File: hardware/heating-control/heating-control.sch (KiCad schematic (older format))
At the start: 10 parts

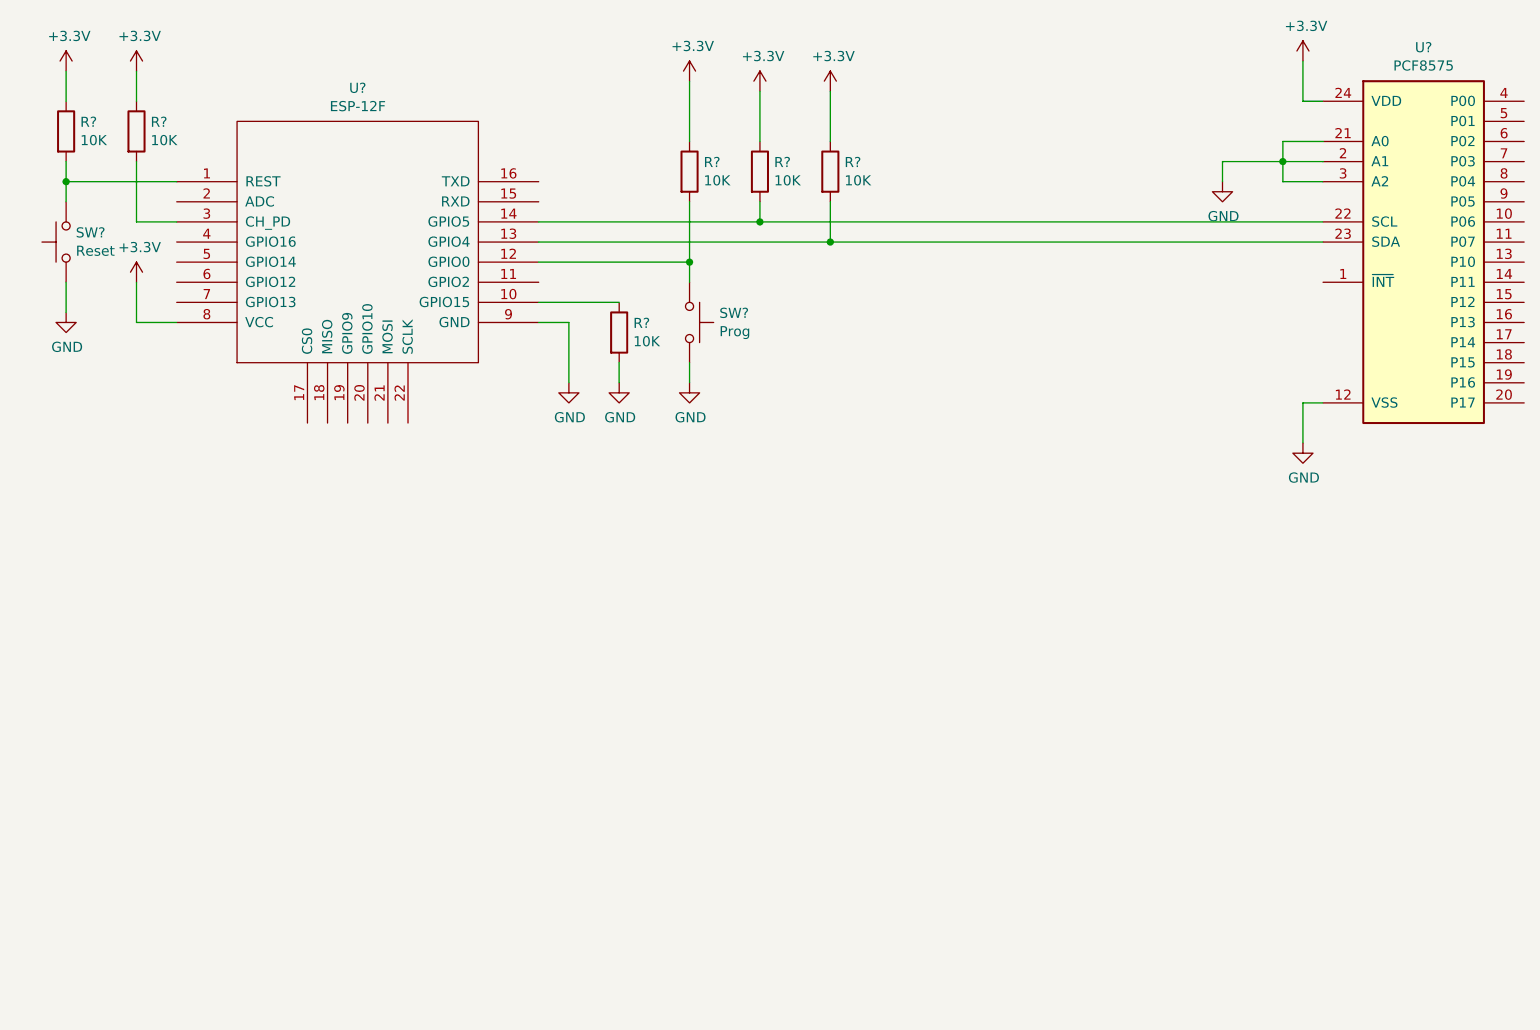
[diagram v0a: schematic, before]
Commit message: added programming interface
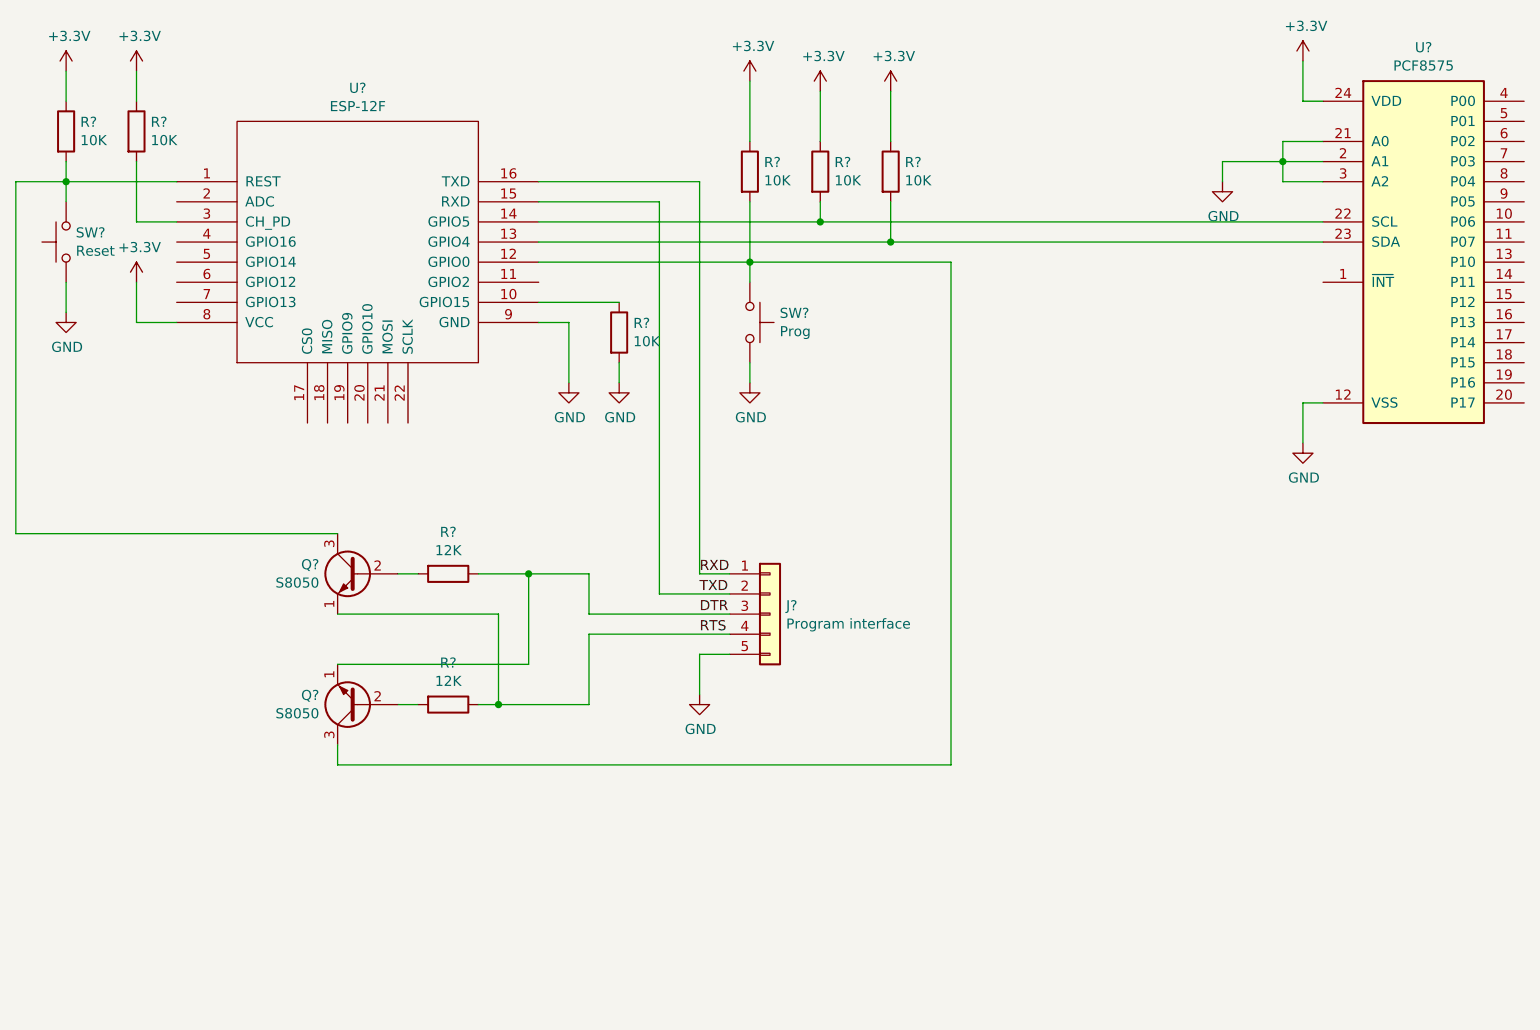
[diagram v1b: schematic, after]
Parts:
- removed R?: 10K, symbol Device:R
- added J?: Program interface, symbol Connector_Generic:Conn_01x05
- added Q? (x2): S8050, Package_TO_SOT_THT:TO-92_Inline, symbol Transistor_BJT:S8050
- added R? (x2): 12K, symbol Device:R
- added R?: 10K, symbol Device:R
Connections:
- net +3V3: now also R?.1
- net GND: now also J?.5 (Pin_5)
- net at SW?.2, U?.1 (REST): now also Q?.3 (C), R?.2
- net at R?.2, SW?.1, U?.12 (GPIO0): now also Q?.3 (C)
- net TXD: now reaches U?.15 (RXD)
- net TXD: now also J?.2 (Pin_2)
- net RXD: now reaches U?.16 (TXD)
- net RXD: now also J?.1 (Pin_1)
- new net: Q?.2 (B), R?.2 (x2)
- new net DTR: J?.3 (Pin_3), Q?.1 (E), R?.1
- new net RTS: J?.4 (Pin_4), Q?.1 (E), R?.1
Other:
- moved on the sheet: R?, SW?

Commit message: a lot of progress in hardware design
separated different board into separate hierarchical schematics
hierarchical schematics for parts to be multiplied
separate project files for each board for creating separate PCBs without interconnection
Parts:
- removed J?: Program interface, symbol Connector_Generic:Conn_01x05
- removed Q? (x2): S8050, Package_TO_SOT_THT:TO-92_Inline, symbol Transistor_BJT:S8050
- removed R? (x6): 10K, symbol Device:R
- removed R? (x2): 12K, symbol Device:R
- removed SW?: Reset, symbol Switch:SW_Push
- removed SW?: Prog, symbol Switch:SW_Push
- removed U?: ESP-12F, symbol ESP8266:ESP-12F
- removed U?: PCF8575, IPC7351-Nominal:SOP65P775X200-24, symbol NXP:PCF8575
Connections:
- net labels added: +12V
- net labels removed: +3.3V, DTR, RTS, RXD, TXD
- wire segments 67 -> 5
